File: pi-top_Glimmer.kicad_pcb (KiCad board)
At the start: 4 copper layers, 65 x 56 mm, 107 parts, among them J1 CONN_01X06, J2 CONN_02X03, J3 CONN_02X17, J4 CONN_02X20, J5 CONN_02X17, J6 CONN_02X01, Q1 IRFML8244, Q2 IRFML8244, Q3 IRFML8244, Q4 IRFML8244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

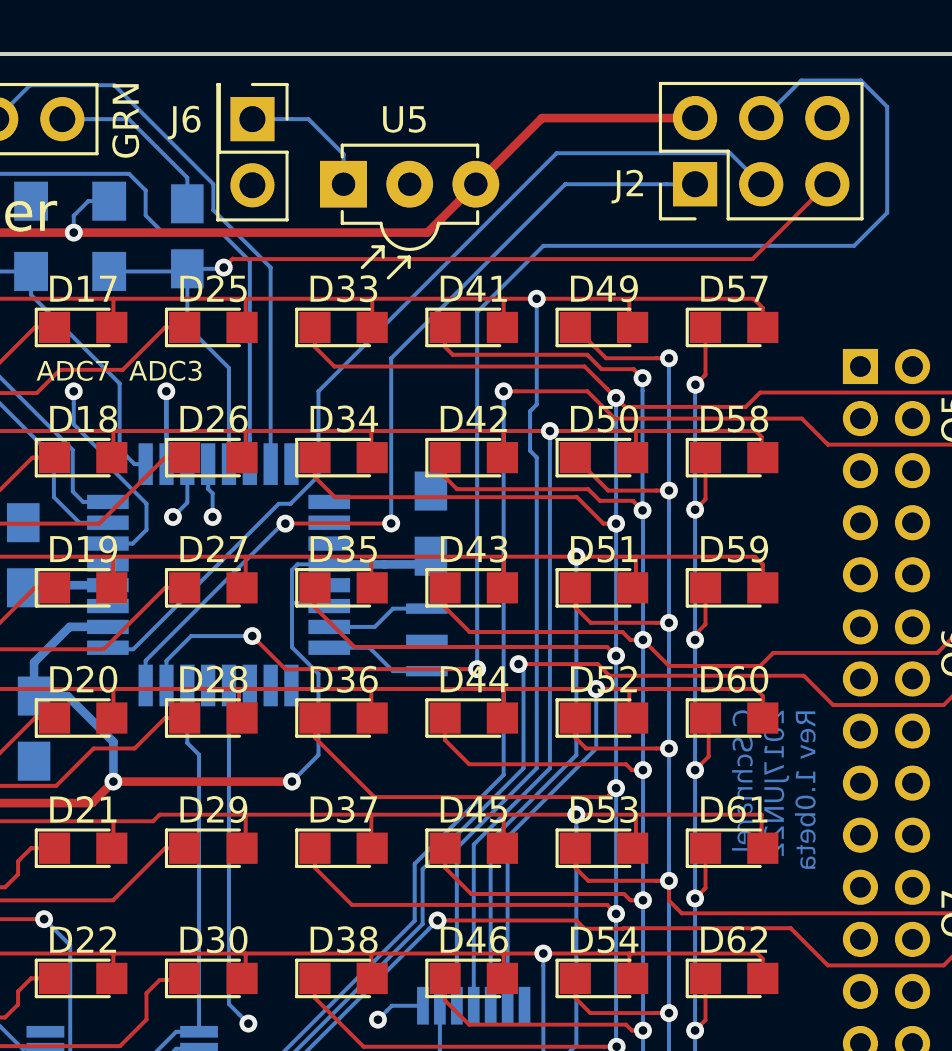
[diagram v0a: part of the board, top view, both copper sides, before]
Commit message: Added solder jumper to IR Rcvr; README edits
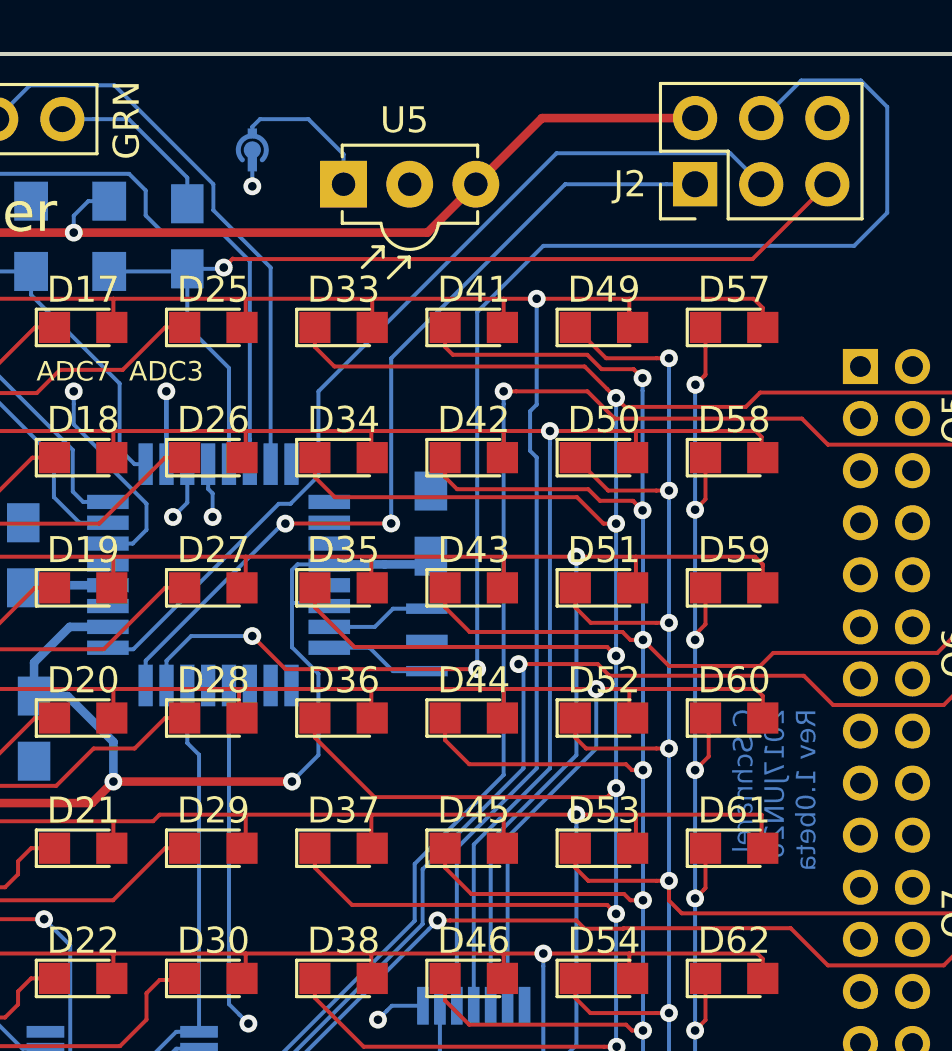
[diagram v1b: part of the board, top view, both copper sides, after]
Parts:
- J6: value CONN_02X01 -> SPST_Jumper; footprint Pin_Headers:Pin_Header_Straight_2x01_Pitch2.54mm -> SolderJumpers:SPST_Jumper; moved to B.Cu
- U1: value 7215 -> AP7215-33YG
- moved J6 1.18 mm to (69.5, 77.7)
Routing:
- net BCM-17: track 154.9 -> 155.9 mm, vias 0 -> 1
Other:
- board text added: "C.Schnarel 2017JUN26 Rev 1.0beta"
- board text removed: "C.Schnarel 2017JUN22 Rev 1.0beta"
